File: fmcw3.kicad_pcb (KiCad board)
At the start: 6 copper layers, 104 x 47.7 mm, 397 parts, among them CON1 SD_Card_DM3BT, CON2 BARREL_JACK, J1 USB_C_Receptacle_USB2.0, J2 Connector_02x08, P1 SMA, P2 SMA, P5 CONN_01X01, P7 CONN_01X01, P8 CONN_01X01, SW1 B3U-1000P, SW2 B3U-1000P, U1 ADF4158, U10 HMC431LP4, U11 SKY65404, U12 PAT1220-3dB, U13 TRF37A73, U14 TQP5525, U15 SMA, U16 SKY65404, U17 LMR51420, U18 LMR51420, U19 LMR51420, U2 SolderPad_1_Circle, U20 LP5907-3.0, U21 LP2985A-10DBVR, U22 LD3920, U23 LD3920, U24 LD3920, U25 BU33SD5WG, U26 5400BL15B0050001E, U27 5400BL15B0050001E, U28 5400BL15B0050001E, U29 ADL5802, U3 PAT1220-6dB, U30 XC7A35T-1FTG256C, U31 SolderPad_1_Circle, U32 93LC46B, U33 FT2232H, U34 SolderPad_1_Circle, U35 SolderPad_1_Circle, U36 SolderPad_1_Circle, U38 SolderPad_1_Circle, U39 LP5907-3.0, U4 SolderPad_1_Circle, U40 W25Q128JV, U41 SolderPad_1_Circle, U42 SolderPad_1_Circle, U43 SolderPad_1_Circle, U44 SolderPad_1_Circle, U45 LT6232, U46 SolderPad_1_Circle, U47 SolderPad_1_Circle, U48 SolderPad_1_Circle, U49 SolderPad_1_Circle, U5 SolderPad_1_Circle, U6 PL133-37, U7 TLV172DCK, U8 LTC2292, U9 TRF37A73, Y1 ABM10-167-12.000MHZ-T3, Y2 ECS-TXO-32CSMV

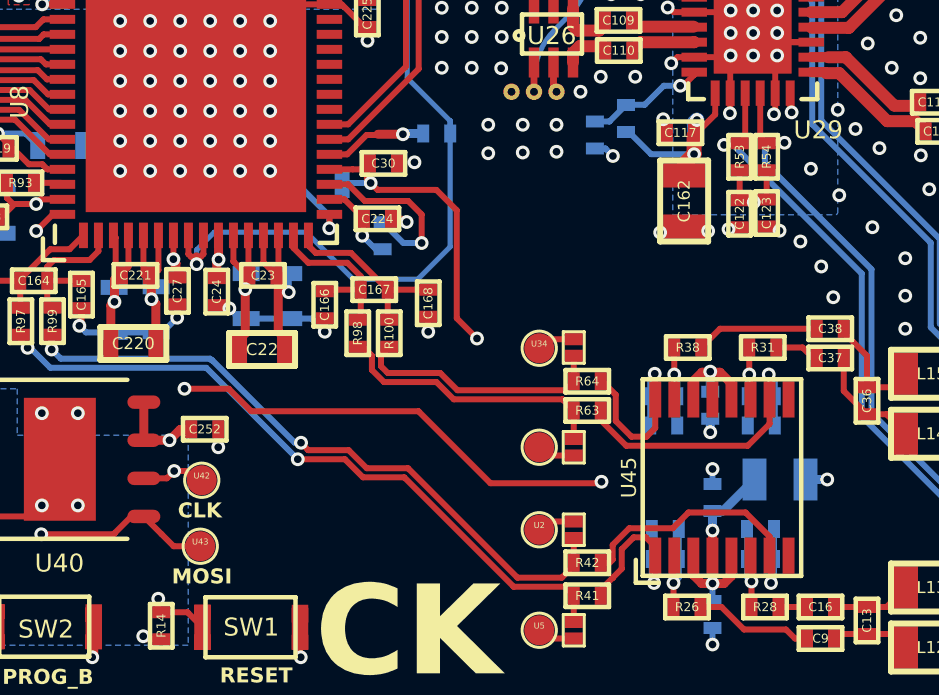
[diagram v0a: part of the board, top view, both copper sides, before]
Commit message: vcom trace width is changed
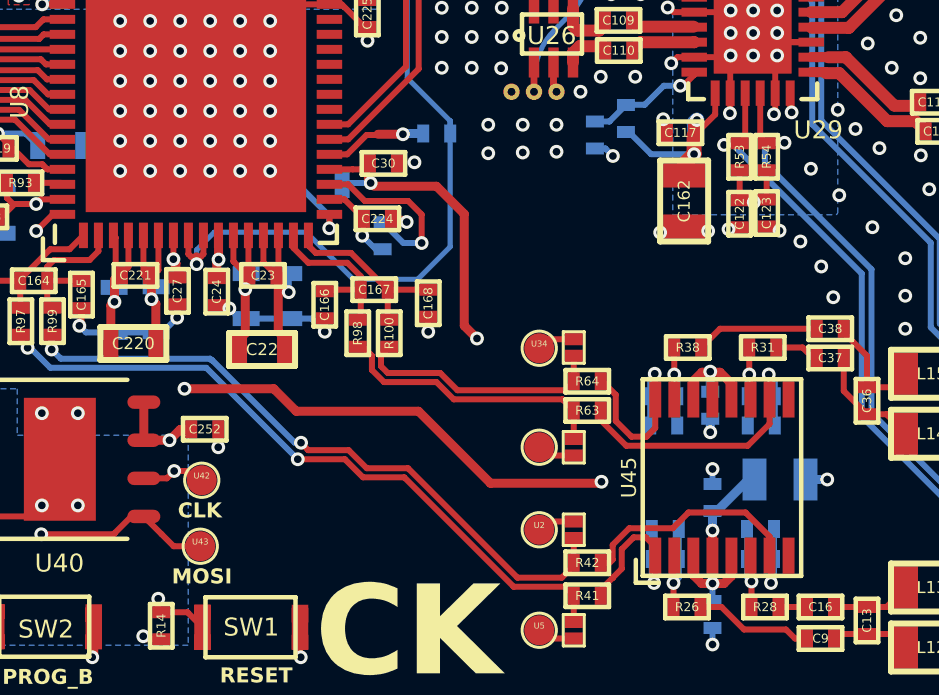
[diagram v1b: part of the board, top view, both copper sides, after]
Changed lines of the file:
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@@
 	)
 	(segment
-		(start 171.725 108.225)
+		(start 172.575 107.175)
 		(end 172.775 107.175)
 		(width 0.3)
@@
 	)
 	(segment
-		(start 171.375 108.225)
-		(end 171.725 108.225)
+		(start 171.525 108.225)
+		(end 172.575 107.175)
 		(width 0.3)
 		(layer "B.Cu")
@@
 	)
 	(segment
+		(start 171.375 108.225)
+		(end 171.525 108.225)
+		(width 0.3)
+		(layer "B.Cu")
+		(net 18)
+	)
+	(segment
 		(start 171.230219 77.93543)
 		(end 171.230219 77.77183)
@@
 	)
 	(segment
-		(start 170.7368 110.3618)
-		(end 171.017302 110.642302)
+		(start 163.525 102.475)
+		(end 163.1 102.05)
 		(width 0.3)
 		(layer "F.Cu")
@@
 	)
 	(segment
-		(start 162.171829 97.521829)
-		(end 160.210218 97.521829)
-		(width 0.2)
-		(layer "F.Cu")
-		(net 389)
-	)
-	(segment
-		(start 162.85 101.8)
-		(end 162.85 98.2)
-		(width 0.2)
+		(start 170.7368 110.3618)
+		(end 171.017302 110.642302)
+		(width 0.3)
 		(layer "F.Cu")
 		(net 389)
@@
 	)
 	(segment
-		(start 160.210218 97.521829)
+		(start 160.088389 97.4)
 		(end 159.980219 97.29183)
 		(width 0.2)
@@
 	)
 	(segment
-		(start 163.525 102.475)
-		(end 162.85 101.8)
-		(width 0.2)
-		(layer "F.Cu")
-		(net 389)
-	)
-	(segment
 		(start 170.7368 109.7107)
 		(end 170.7368 110.3618)
@@
 	)
 	(segment
+		(start 163.1 102.05)
+		(end 163.1 98.325)
+		(width 0.3)
+		(layer "F.Cu")
+		(net 389)
+	)
+	(segment
 		(start 159.855755 96.637524)
 		(end 159.855755 97.167366)
@@
 	)
 	(segment
+		(start 162.175 97.4)
+		(end 160.088389 97.4)
+		(width 0.3)
+		(layer "F.Cu")
+		(net 389)
+	)
+	(segment
 		(start 158.605755 96.837524)
 		(end 159.380219 96.837524)
@@
 	)
 	(segment
-		(start 162.85 98.2)
-		(end 162.171829 97.521829)
-		(width 0.2)
+		(start 163.1 98.325)
+		(end 162.175 97.4)
+		(width 0.3)
 		(layer "F.Cu")
 		(net 389)
@@
 	)
 	(segment
+		(start 153.775 104.15)
+		(end 156.75 104.15)
+		(width 0.3)
+		(layer "F.Cu")
+		(net 390)
+	)
+	(segment
 		(start 172.0068 103.9818)
 		(end 172.0068 104.5107)
@@
 	)
 	(segment
-		(start 156 104.9)
-		(end 161.575 104.9)
+		(start 167.625 107.3)
+		(end 167.675 107.25)
 		(width 0.2)
 		(layer "F.Cu")
@@
 	)
 	(segment
-		(start 167.625 107.3)
-		(end 167.675 107.25)
-		(width 0.2)
+		(start 156.75 104.15)
+		(end 157.5 104.9)
+		(width 0.3)
 		(layer "F.Cu")
 		(net 390)
@@
 	)
 	(segment
-		(start 170.7368 104.5107)
-		(end 170.7368 103.8882)
+		(start 157.5 104.9)
+		(end 161.575 104.9)
 		(width 0.3)
 		(layer "F.Cu")
@@
 	)
 	(segment
-		(start 149.035766 96.667535)
-		(end 149.205755 96.837524)
-		(width 0.2)
+		(start 170.7368 104.5107)
+		(end 170.7368 103.8882)
+		(width 0.3)
 		(layer "F.Cu")
 		(net 390)
 	)
 	(segment
-		(start 153.775 104.15)
-		(end 155.25 104.15)
+		(start 149.035766 96.667535)
+		(end 149.205755 96.837524)
 		(width 0.2)
 		(layer "F.Cu")
@@
 	)
 	(segment
-		(start 149.205755 96.837524)
-		(end 149.705755 96.837524)
-		(width 0.2)
+		(start 161.575 104.9)
+		(end 163.975 107.3)
+		(width 0.3)
 		(layer "F.Cu")
 		(net 390)
@@
 		(start 163.975 107.3)
 		(end 167.625 107.3)
-		(width 0.2)
+		(width 0.3)
 		(layer "F.Cu")
 		(net 390)
 	)
 	(segment
-		(start 155.25 104.15)
-		(end 156 104.9)
+		(start 149.205755 96.837524)
+		(end 149.705755 96.837524)
 		(width 0.2)
 		(layer "F.Cu")
@@
 		(net 390)
 	)
-	(segment
-		(start 161.575 104.9)
-		(end 163.975 107.3)
-		(width 0.2)
-		(layer "F.Cu")
-		(net 390)
-	)
 	(via
 		(at 171.3 103.579098)
@@
 		(start 148.3 104.15)
 		(end 147.5 103.35)
-		(width 0.2)
+		(width 0.3)
 		(layer "In3.Cu")
 		(net 390)
@@
 		(start 147.5 100)
 		(end 148.1 99.4)
-		(width 0.2)
+		(width 0.3)
 		(layer "In3.Cu")
 		(net 390)
@@
 		(start 148.1 96.191331)
 		(end 147.55 95.641331)
-		(width 0.2)
+		(width 0.3)
 		(layer "In3.Cu")
 		(net 390)
@@
 		(start 153.775 104.15)
 		(end 148.3 104.15)
-		(width 0.2)
+		(width 0.3)
 		(layer "In3.Cu")
 		(net 390)
@@
 		(start 148.1 99.4)
 		(end 148.1 96.191331)
-		(width 0.2)
+		(width 0.3)
 		(layer "In3.Cu")
 		(net 390)
@@
 		(start 147.5 103.35)
 		(end 147.5 100)
-		(width 0.2)
+		(width 0.3)
 		(layer "In3.Cu")
 		(net 390)
@@
 			)
 		)
+	)
+	(zone
+		(net 0)
+		(net_name "")
+		(layers "F.Cu" "B.Cu")
+		(hatch edge 0.5)
+		(connect_pads
+			(clearance 0)
+		)
+		(min_thickness 0.25)
+		(filled_areas_thickness no)
+		(keepout
+			(tracks allowed)
+			(vias allowed)
+			(pads allowed)
+			(copperpour not_allowed)
+			(footprints allowed)
+		)
+		(placement
+			(enabled no)
+			(sheetname "/clock/")
+		)
+		(fill
+			(thermal_gap 0.5)
+			(thermal_bridge_width 0.5)
+		)
+		(polygon
+			(pts
+				(xy 171.8 103.226292) (xy 171.8 106.176292) (xy 174.2 106.176292) (xy 174.2 103.226292)
+			)
+		)
+	)
+	(zone
+		(net 0)
+		(net_name "")
+		(layers "F.Cu" "B.Cu")
+		(hatch edge 0.5)
+		(connect_pads
+			(clearance 0)
+		)
+		(min_thickness 0.25)
+		(filled_areas_thickness no)
+		(keepout
+			(tracks allowed)
+			(vias allowed)
+			(pads allowed)
+			(copperpour not_allowed)
+			(footprints allowed)
+		)
+		(placement
+			(enabled no)
+			(sheetname "/clock/")
+		)
+		(fill
+			(thermal_gap 0.5)
+			(thermal_bridge_width 0.5)
+		)
+		(polygon
+			(pts
+				(xy 171.8 107.95) (xy 171.8 110.9) (xy 174.2 110.9) (xy 174.2 107.95)
+			)
+		)
+	)
+	(zone
+		(net 0)
+		(net_name "")
+		(layers "F.Cu" "B.Cu")
+		(hatch edge 0.5)
+		(connect_pads
+			(clearance 0)
+		)
+		(min_thickness 0.25)
+		(filled_areas_thickness no)
+		(keepout
+			(tracks allowed)
+			(vias allowed)
+			(pads allowed)
+			(copperpour not_allowed)
+			(footprints allowed)
+		)
+		(placement
+			(enabled no)
+			(sheetname "/clock/")
+		)
+		(fill
+			(thermal_gap 0.5)
+			(thermal_bridge_width 0.5)
+		)
+		(polygon
+			(pts
+				(xy 168.6 103.222676) (xy 168.6 106.172676) (xy 170.95 106.172676) (xy 170.95 103.222676)
+			)
+		)
+	)
+	(zone
+		(net 0)
+		(net_name "")
+		(layers "F.Cu" "B.Cu")
+		(hatch edge 0.5)
+		(connect_pads
+			(clearance 0)
+		)
+		(min_thickness 0.25)
+		(filled_areas_thickness no)
+		(keepout
+			(tracks allowed)
+			(vias allowed)
+			(pads allowed)
+			(copperpour not_allowed)
+			(footprints allowed)
+		)
+		(placement
+			(enabled no)
+			(sheetname "/clock/")
+		)
+		(fill
+			(thermal_gap 0.5)
+			(thermal_bridge_width 0.5)
+		)
+		(polygon
+			(pts
+				(xy 168.55 107.941561) (xy 168.55 110.891561) (xy 171.05 110.891561) (xy 171.05 107.941561)
+			)
+		)
